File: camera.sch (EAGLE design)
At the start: 10 parts

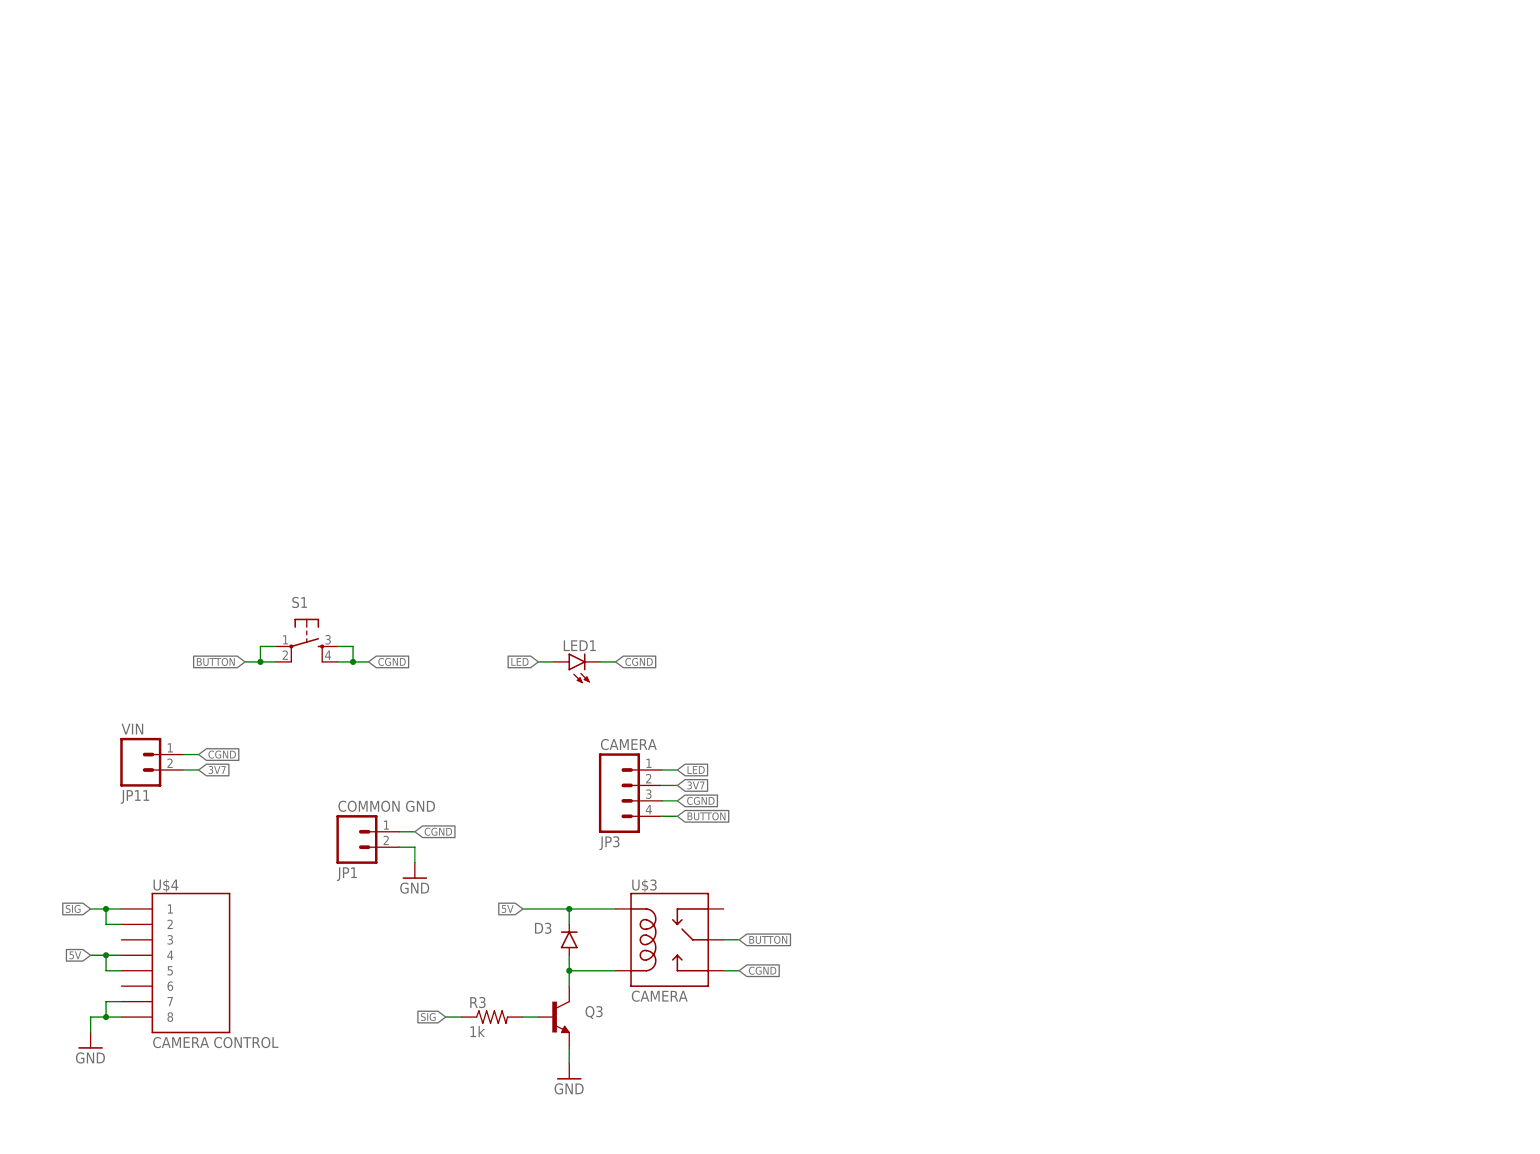
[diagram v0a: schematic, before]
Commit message: Significantly reduce board footprint
Significant reduction in board footprint as the result of moving relay
and related electronic components to the supporting Galactic Aztec RPi
Add-on: Valve + Camera Control board.
Components that remain on this board were replaced with SMD versions.
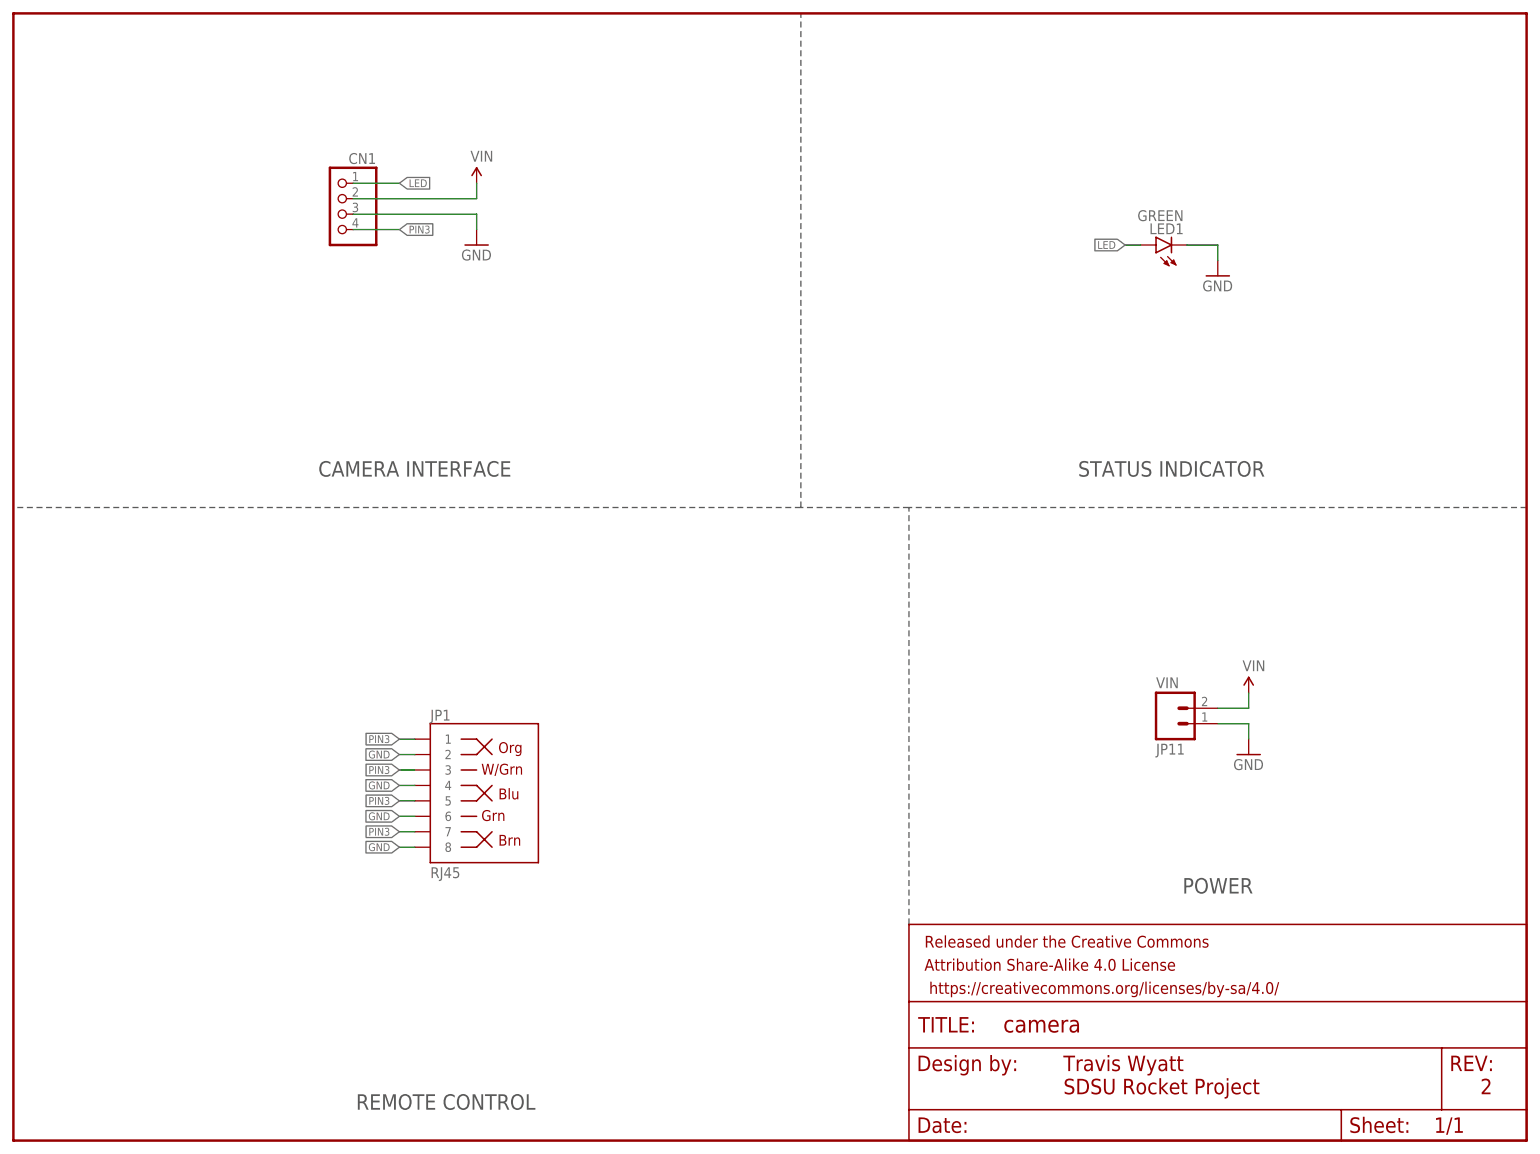
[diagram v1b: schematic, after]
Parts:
- removed D3: (no value), SparkFun-DiscreteSemi:DIODEPTH
- removed JP3: CAMERA, SparkFun-Connectors:M04JST-PTH
- removed Q3: (no value), SparkFun-DiscreteSemi:TRANSISTOR_NPNP2N2222A
- removed R3: 1k, SparkFun-Resistors:1KOHM1/4W5%(PTH)
- removed S1: (no value), SparkFun-Electromechanical:TAC_SWITCHPTH
- removed U$3: CAMERA, SparkFun-Electromechanical:RELAYPTH
- removed U$4: CAMERA CONTROL, SparkFun-Connectors:RJ45-8PTH
- added CN1: (no value), microbuilder_v2:JST_4PIN
- added FRAME1: (no value), SparkFun-Aesthetics:FRAME-LETTER
- JP1: value COMMON GND -> RJ45; device SparkFun-Connectors:M02PTH -> SparkFun-Connectors:RJ45-8PTH
- JP11: device SparkFun-Connectors:M02JST-PTH-2 -> SparkFun-Connectors:M02-JST-2MM-SMT
- LED1: value (none) -> GREEN; device SparkFun-LED:LED3MM -> SparkFun-LED:LED-GREEN0603
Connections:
- removed net 3V7: JP11.2, JP3.2
- removed net 5V: D3.C, U$3.COIL1, U$4.4, U$4.5
- removed net BUTTON: JP3.4, S1.1, S1.2, U$3.MAIN
- removed net CGND: JP1.1, JP11.1, JP3.3, LED1.C, S1.3, S1.4, U$3.NO
- removed net N$11: D3.A, Q3.C, U$3.COIL2
- removed net N$5: Q3.B, R3.2
- removed net SIG: R3.1, U$4.1, U$4.2
- new net PIN3: CN1.4, JP1.1, JP1.3, JP1.5, JP1.7
- new net VIN: CN1.2, JP11.1
- net GND: now also CN1.3, JP1.4, JP1.6, JP1.8, JP11.2, LED1.C; no longer Q3.E, U$4.7, U$4.8
- net LED: now also CN1.1; no longer JP3.1
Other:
- note added: "2"
- note added: "CAMERA INTERFACE"
- note added: "POWER"
- note added: "REMOTE CONTROL"
- note added: "SDSU Rocket Project"
- note added: "STATUS INDICATOR"
- note added: "Travis Wyatt"
- moved on the sheet: JP11, LED1
